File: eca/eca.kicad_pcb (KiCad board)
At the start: 2 copper layers, 60 x 61.5 mm, 22 parts, among them J1 RPI Bus, J10 ESP32CAM Power Supply Bus, J11 28BYJ48 1 Power Supply Bus, J12 28BYJ48 2 Power Supply Bus, J13 28BYJ48 3 Power Supply Bus, J2 GY 906 Bus, J3 MAX30102 Bus, J5 TCRT5000 2 Bus, J7 28BYJ48 1 Control Bus, J8 28BYJ48 2 Control Bus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

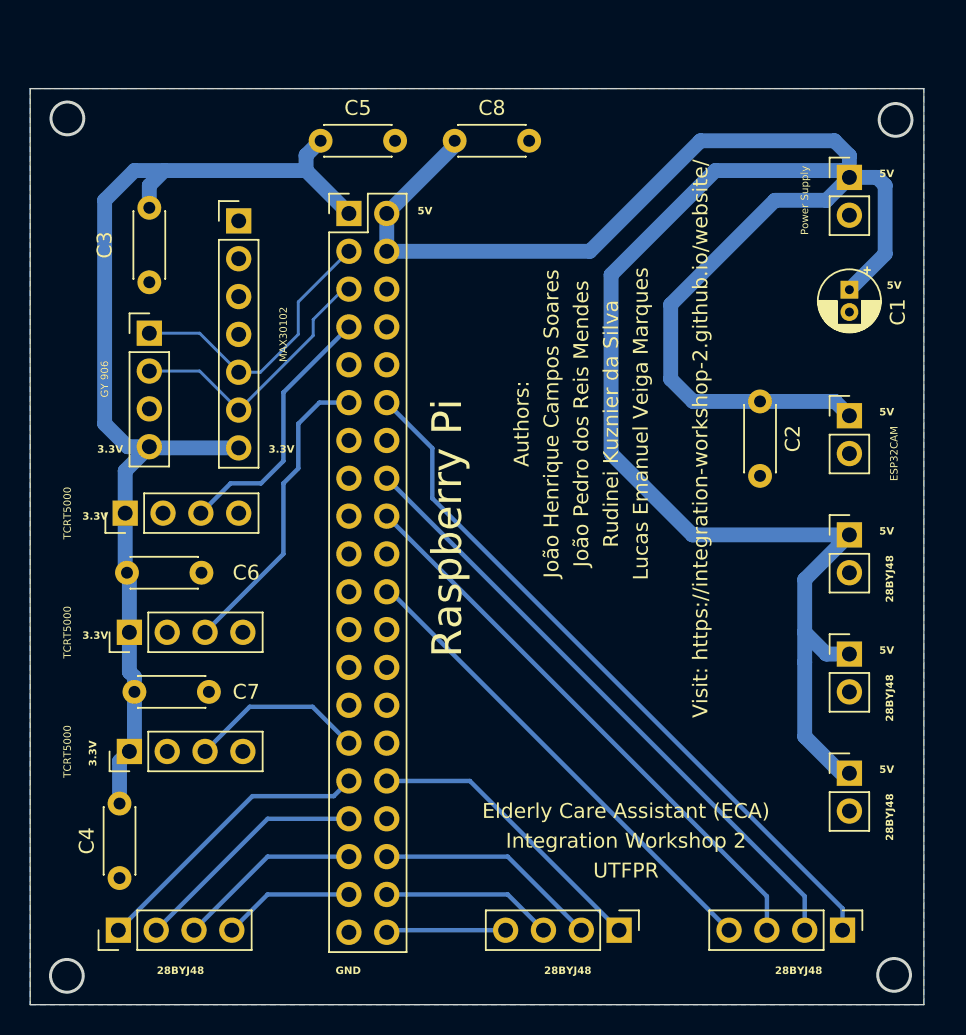
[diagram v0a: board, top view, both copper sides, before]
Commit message: modified pads and tracks sizes
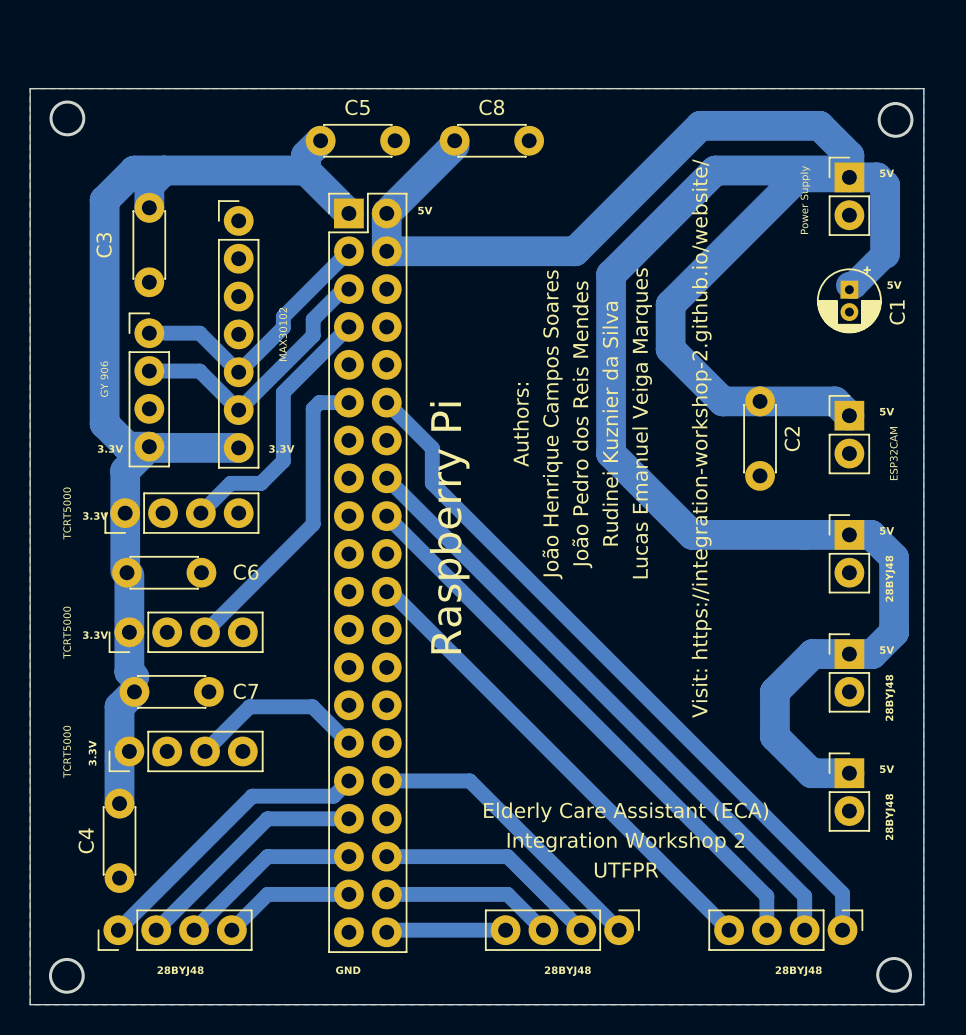
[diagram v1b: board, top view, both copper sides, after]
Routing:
- net 5V: track 161.4 -> 167.3 mm
- net 3.3V: track 73.8 -> 75.2 mm
- net GPIO2: track 19.1 -> 18.3 mm

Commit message: added fan bus
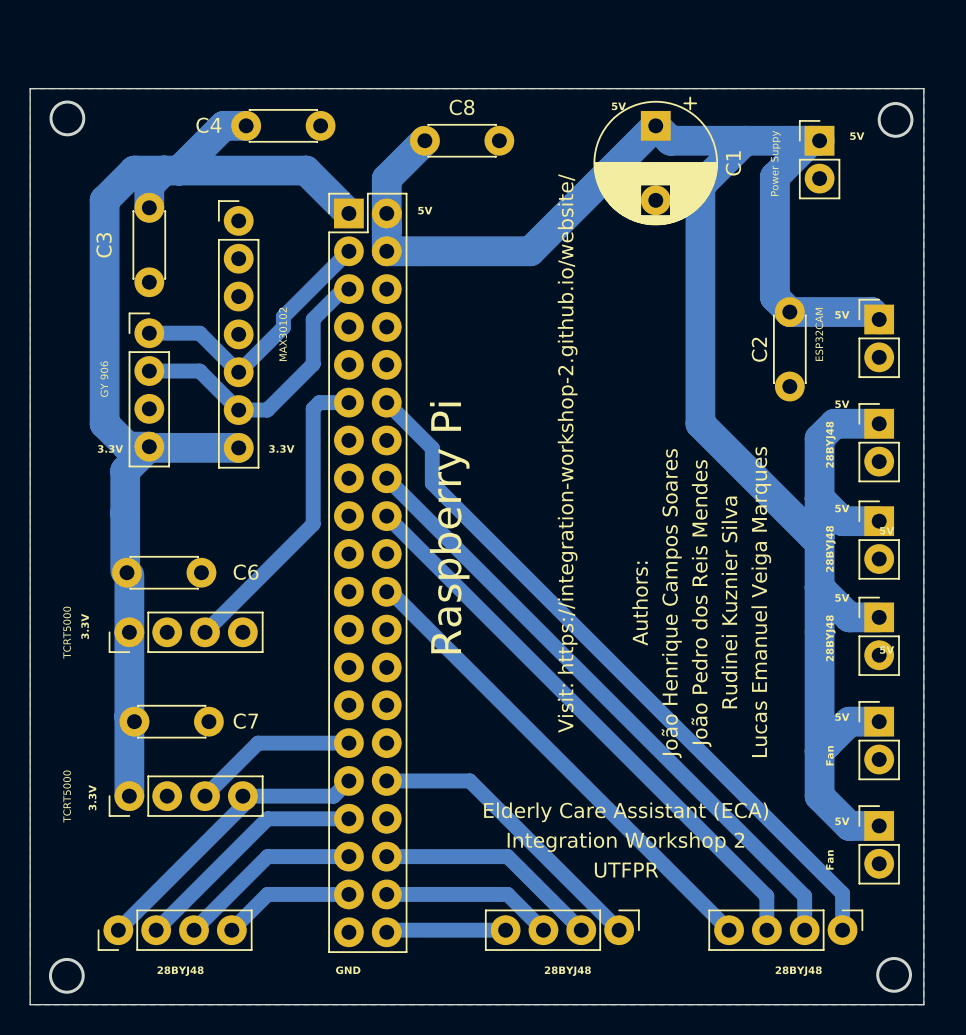
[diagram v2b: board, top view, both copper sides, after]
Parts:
- removed C5: 100nF, Capacitor_THT:C_Disc_D4.3mm_W1.9mm_P5.00mm
- removed TCRT5000: TCRT5000 3 Bus, Connector_PinHeader_2.54mm:PinHeader_1x04_P2.54mm_Vertical
- added J15: Fan 1 Power Supply Bus, Connector_PinHeader_2.54mm:PinHeader_1x02_P2.54mm_Vertical, F.Cu at (157.0, 121.0)
- added J16: Fan Power Supply Bus, Connector_PinHeader_2.54mm:PinHeader_1x02_P2.54mm_Vertical, F.Cu at (157.0, 114.0)
- C1: footprint Capacitor_THT:CP_Radial_D4.0mm_P1.50mm -> Capacitor_THT:CP_Radial_D8.0mm_P5.00mm
- Power Suppy: renamed from Power Supply
- moved C4 52.3 mm to (119.5, 74.0), turned to 180 degrees
- moved C1 17.0 mm to (142.0, 74.0)
- moved J11 10.6 mm to (157.0, 107.0)
- moved J12 9.14 mm to (157.0, 100.5)
- moved J13 7.72 mm to (157.0, 94.0)
- moved J10 6.76 mm to (157.0, 87.0)
- moved C2 6.32 mm to (151.0, 86.5)
- moved Power Suppy 3.17 mm to (153.0, 75.0)
- moved J4 3.00 mm to (106.7, 119.0)
- moved C7 2.00 mm to (107.0, 114.0)
- moved C8 2.00 mm to (126.5, 75.0)
- renumbered TCRT5000 to J4
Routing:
- net 5V: track 167.3 -> 142.1 mm
- net GPIO4: track 17.8 -> 0.00 mm
- net 3.3V: track 75.2 -> 77.0 mm
- net GPIO3: track 18.5 -> 19.6 mm
- net GPIO5: track 12.1 -> 11.3 mm
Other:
- board text added: "Fan"
- board text added: "Rudinei Kuznier Silva"
- board text removed: "Rudinei Kuznier da Silva"

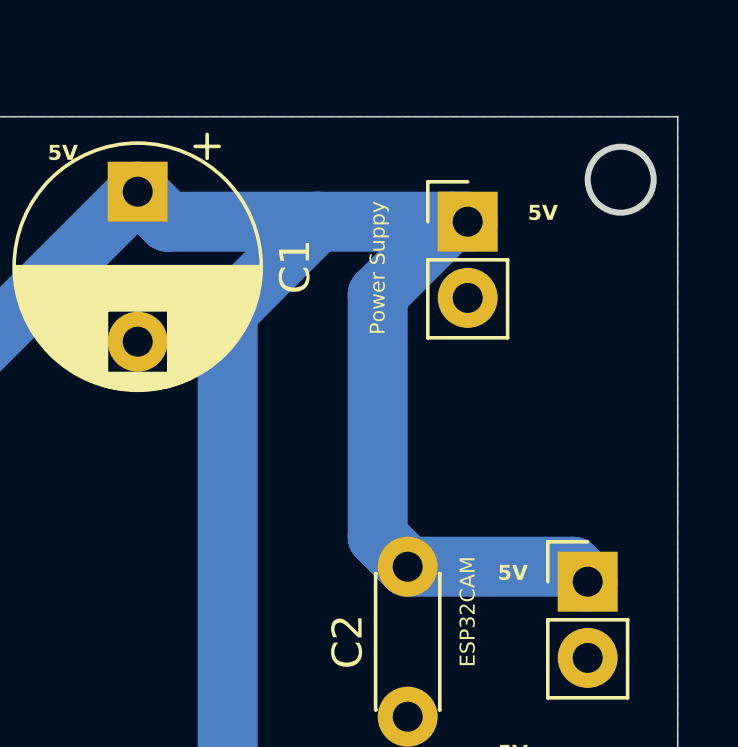
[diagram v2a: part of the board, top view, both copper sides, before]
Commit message: changed input connector
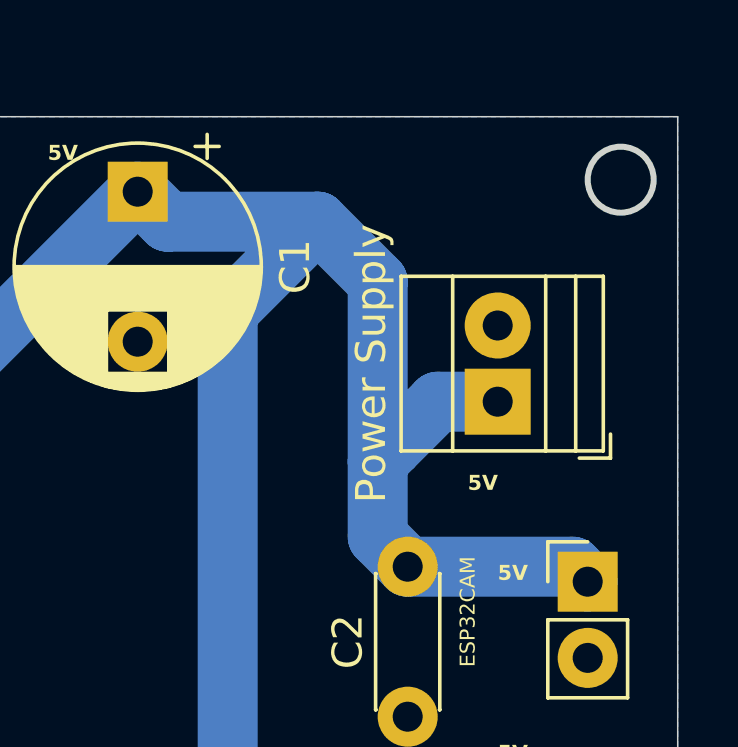
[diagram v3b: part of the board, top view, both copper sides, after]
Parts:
- Power Supply: renamed from Power Suppy; footprint Connector_PinHeader_2.54mm:PinHeader_1x02_P2.54mm_Vertical -> TerminalBlock:TerminalBlock_Xinya_XY308-2.54-2P_1x02_P2.54mm_Horizontal
- moved Power Supply 6.08 mm to (154.0, 81.0), turned to 90 degrees
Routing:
- net 5V: track 142.1 -> 141.2 mm

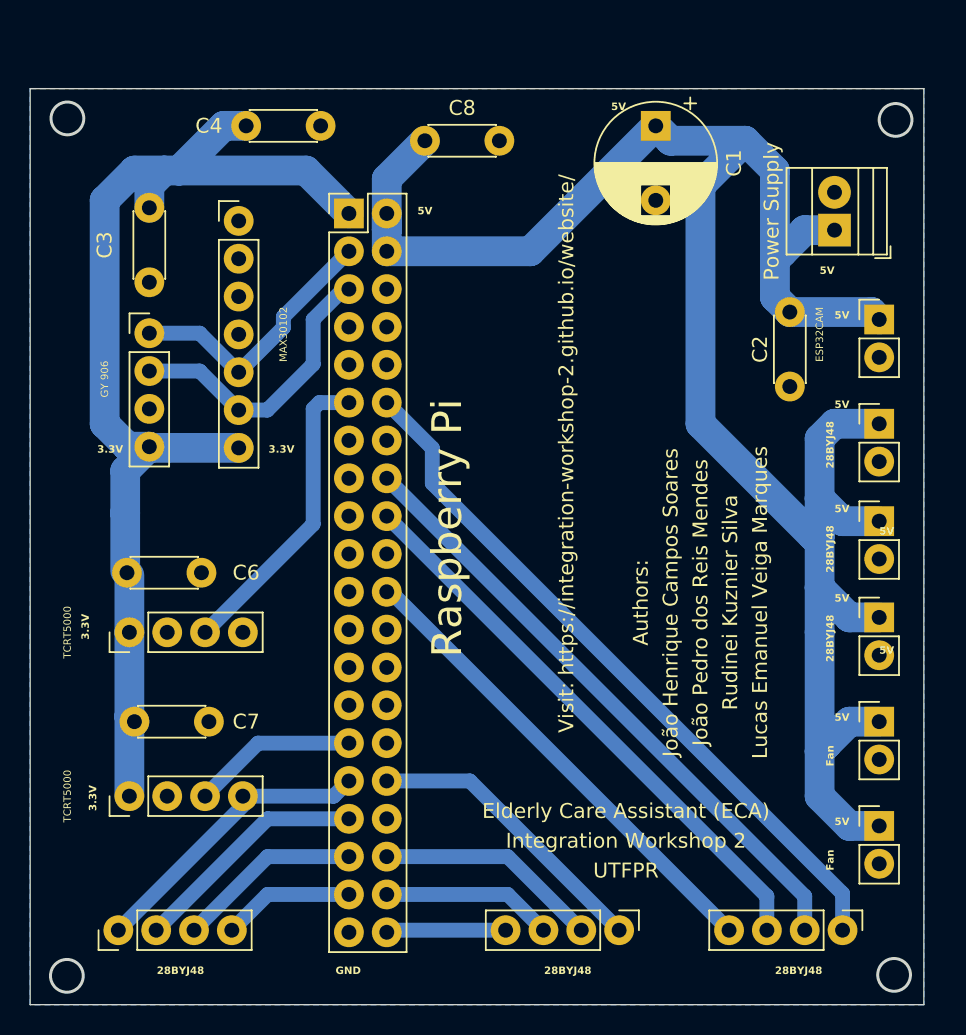
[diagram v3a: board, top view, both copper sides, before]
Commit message: changed power supply connector
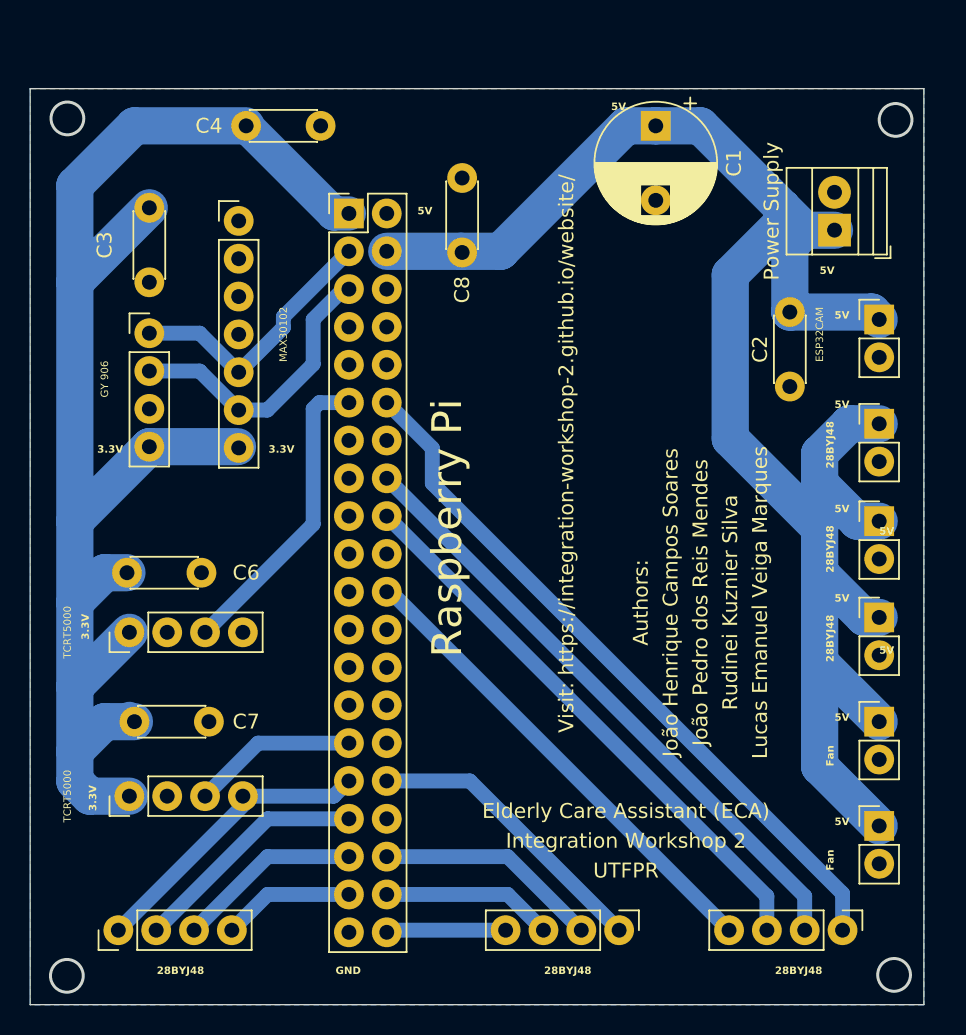
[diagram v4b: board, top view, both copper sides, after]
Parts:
- moved C8 7.91 mm to (129.0, 82.5), turned to 90 degrees
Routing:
- net 3.3V: track 77.0 -> 102.6 mm
- net 5V: track 141.2 -> 122.5 mm

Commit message: alpha version
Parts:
- removed C3, C4: 100nF, Capacitor_THT:C_Disc_D4.3mm_W1.9mm_P5.00mm
- removed Power Supply: Power Supply Input, TerminalBlock:TerminalBlock_Xinya_XY308-2.54-2P_1x02_P2.54mm_Horizontal
- added J6: Power Supply Input, TerminalBlock:TerminalBlock_Xinya_XY308-2.54-3P_1x03_P2.54mm_Horizontal, F.Cu at (107.8, 81.5)
- moved J10 52.0 mm to (105.0, 87.5)
- moved J11 52.0 mm to (105.0, 107.5)
- moved J12 52.0 mm to (105.0, 101.0)
- moved J13 52.0 mm to (105.0, 94.5)
- moved J15 52.0 mm to (105.0, 121.5)
- moved J16 52.0 mm to (105.0, 114.5)
- moved J4 46.7 mm to (152.8, 112.0), turned to -90 degrees
- moved C6 46.5 mm to (152.5, 97.0), turned to 180 degrees
- moved J5 46.3 mm to (152.6, 102.0), turned to -90 degrees
- moved J7 46.2 mm to (152.1, 129.0), turned to -90 degrees
- moved J8 45.7 mm to (108.8, 129.0), turned to 90 degrees
- moved C7 45.7 mm to (152.5, 118.0), turned to 180 degrees
- moved C2 41.0 mm to (110.0, 86.5)
- moved J3 39.1 mm to (153.0, 77.4)
- moved J2 35.8 mm to (143.0, 80.5)
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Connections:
- J1 pad 1: 3.3V -> 5V
- J1 pad 10: GPIO15 -> GND
- J1 pad 11: GPIO17 -> GPIO18
- J1 pad 12: GPIO18 -> GPIO17
- J1 pad 13: GPIO27 -> GND
- J1 pad 14: GND -> GPIO27
- J1 pad 15: GPIO22 -> GPIO23
- J1 pad 16: GPIO23 -> GPIO22
- J1 pad 17: 3.3V -> GPIO24
- J1 pad 18: GPIO24 -> 3.3V
- J1 pad 19: GPIO10 -> GND
- J1 pad 2: 5V -> 3.3V
- J1 pad 20: GND -> GPIO10
- J1 pad 21: GPIO9 -> GPIO25
- J1 pad 22: GPIO25 -> GPIO9
- J1 pad 23: GPIO11 -> GPIO8
- J1 pad 24: GPIO8 -> GPIO11
- J1 pad 25: GND -> GPIO7
- J1 pad 26: GPIO7 -> GND
- J1 pad 27: ID_SD -> ID_SC
- J1 pad 28: ID_SC -> ID_SD
- J1 pad 29: GPIO5 -> GND
- J1 pad 3: GPIO2 -> 5V
- J1 pad 30: GND -> GPIO5
- J1 pad 31: GPIO6 -> GPIO12
- J1 pad 32: GPIO12 -> GPIO6
- J1 pad 33: GPIO13 -> GND
- J1 pad 34: GND -> GPIO13
- J1 pad 35: GPIO19 -> GPIO16
- J1 pad 36: GPIO16 -> GPIO19
- J1 pad 37: GPIO26 -> GPIO20
- J1 pad 38: GPIO20 -> GPIO26
- J1 pad 39: GND -> GPIO21
- J1 pad 4: 5V -> GPIO2
- J1 pad 40: GPIO21 -> GND
- J1 pad 5: GPIO3 -> GND
- J1 pad 6: GND -> GPIO3
- J1 pad 7: GPIO4 -> GPIO14
- J1 pad 8: GPIO14 -> GPIO4
- J1 pad 9: GND -> GPIO15
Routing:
- net 3.3V: track 102.6 -> 60.8 mm
- net GPIO2: track 18.3 -> 23.2 mm
- net GPIO17: track 20.6 -> 15.7 mm
- net 5V: track 122.5 -> 118.5 mm
- net GPIO21: track 8.04 -> 5.12 mm
- net GPIO20: track 11.5 -> 8.71 mm
- net GPIO16: track 15.1 -> 12.3 mm
- net GPIO12: track 19.8 -> 17.0 mm
- net GPIO5: track 11.3 -> 13.6 mm
- net GPIO3: track 19.6 -> 21.1 mm
- net GPIO6: track 19.6 -> 21.0 mm
- net GPIO26: track 8.85 -> 10.2 mm
- net GPIO19: track 12.4 -> 13.8 mm
- net GPIO13: track 16.0 -> 17.4 mm
- net GPIO25: track 32.4 -> 31.5 mm
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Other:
- board size 60 x 61.5 mm -> 60 x 60 mm
- board text added: "C1"
- board text added: "C2"
- board text added: "C6"
- board text added: "C7"
- board text added: "C8"
- board text added: "GPIO21"
- board text added: "Power Supply"
